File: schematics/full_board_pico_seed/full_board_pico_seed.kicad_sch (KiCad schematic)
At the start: 32 parts, among them J10 Conn_02x20_Odd_Even, J2 Conn_01x02_Male, J9 Conn_01x03, P0 25k, P1 25k, P2 25k, SW4 Enter, SW5 Exit, U12 128X64 OLED Display, U14 AP63205WU, U3 LM1117DT-5.0, U7 MC78M05_TO252

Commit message: minor corrections
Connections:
- net GND: no longer J10.10 (Pin_10), U12.4 (CS)
- new net: J10.10 (Pin_10), U12.4 (CS)
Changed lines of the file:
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@@
   (junction (at 142.24 134.62) (diameter 0) (color 0 0 0 0)
   )
-  (junction (at 62.23 121.92) (diameter 0) (color 0 0 0 0)
-  )
   (junction (at 208.28 72.39) (diameter 0) (color 0 0 0 0)
   )
   (junction (at 237.49 80.01) (diameter 0) (color 0 0 0 0)
-  )
-  (junction (at 62.23 125.73) (diameter 0) (color 0 0 0 0)
   )
   (junction (at 68.58 114.3) (diameter 0) (color 0 0 0 0)
@@
     (stroke (width 0) (type default))
   )
-  (wire (pts (xy 62.23 121.92) (xy 62.23 125.73))
+  (wire (pts (xy 62.23 102.87) (xy 62.23 181.61))
     (stroke (width 0) (type default))
   )
@@
     (stroke (width 0) (type default))
   )
+  (wire (pts (xy 59.69 121.92) (xy 57.15 121.92))
+    (stroke (width 0) (type default))
+  )
   (wire (pts (xy 52.07 128.27) (xy 40.64 128.27))
     (stroke (width 0) (type default))
@@
     (stroke (width 0) (type default))
   )
-  (wire (pts (xy 62.23 102.87) (xy 62.23 121.92))
-    (stroke (width 0) (type default))
-  )
   (wire (pts (xy 233.68 72.39) (xy 237.49 72.39))
     (stroke (width 0) (type default))
@@
     (stroke (width 0) (type default))
   )
-  (wire (pts (xy 62.23 125.73) (xy 62.23 181.61))
-    (stroke (width 0) (type default))
-  )
   (wire (pts (xy 90.17 118.11) (xy 105.41 118.11))
     (stroke (width 0) (type default))
@@
   )
   (wire (pts (xy 81.28 82.55) (xy 92.71 82.55))
-    (stroke (width 0) (type default))
-  )
-  (wire (pts (xy 62.23 121.92) (xy 57.15 121.92))
     (stroke (width 0) (type default))
   )
@@
     )
   )
-  (symbol (lib_id "power:GND") (at 62.23 125.73 0) (mirror y) (unit 1)
-    (in_bom yes) (on_board yes) (dnp no)
-    (property "Reference" "#PWR040" (at 62.23 132.08 0)
-      (effects (font (size 1.27 1.27)) hide)
-    )
-    (property "Value" "GND" (at 59.69 129.54 90)
-      (effects (font (size 1.27 1.27)))
-    )
-    (property "Footprint" "" (at 62.23 125.73 0)
-      (effects (font (size 1.27 1.27)) hide)
-    )
-    (property "Datasheet" "" (at 62.23 125.73 0)
-      (effects (font (size 1.27 1.27)) hide)
-    )
+  (symbol (lib_id "power:GND") (at 59.69 121.92 0) (mirror y) (unit 1)
+    (in_bom yes) (on_board yes) (dnp no)
+    (property "Reference" "#PWR040" (at 59.69 128.27 0)
+      (effects (font (size 1.27 1.27)) hide)
+    )
+    (property "Value" "GND" (at 59.69 120.65 0)
+      (effects (font (size 1.27 1.27)))
+    )
+    (property "Footprint" "" (at 59.69 121.92 0)
+      (effects (font (size 1.27 1.27)) hide)
+    )
+    (property "Datasheet" "" (at 59.69 121.92 0)
+      (effects (font (size 1.27 1.27)) hide)
+    )

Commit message: pcd: changed innductor footprint
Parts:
- L1: footprint Inductor_SMD:L_1812_4532Metric_Pad1.30x3.40mm_HandSolder -> Inductor_SMD:L_Bourns_SRP7028A_7.3x6.6mm
- U3: footprint Package_TO_SOT_SMD:TO-252-3_TabPin2 -> Package_TO_SOT_SMD:TO-252-2
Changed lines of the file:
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@@
       (effects (font (size 1.27 1.27)))
     )
-    (property "Footprint" "Inductor_SMD:L_1812_4532Metric_Pad1.30x3.40mm_HandSolder" (at 252.73 92.71 0)
+    (property "Footprint" "Inductor_SMD:L_Bourns_SRP7028A_7.3x6.6mm" (at 252.73 92.71 0)
       (effects (font (size 1.27 1.27)) hide)
     )
@@
       (effects (font (size 1.27 1.27)))
     )
-    (property "Footprint" "Package_TO_SOT_SMD:TO-252-3_TabPin2" (at 251.46 72.39 0)
-      (effects (font (size 1.27 1.27)) hide)
-    )
+    (property "Footprint" "Package_TO_SOT_SMD:TO-252-2" (at 251.46 72.39 0)
+      (effects (font (size 1.27 1.27)) hide)
+    )

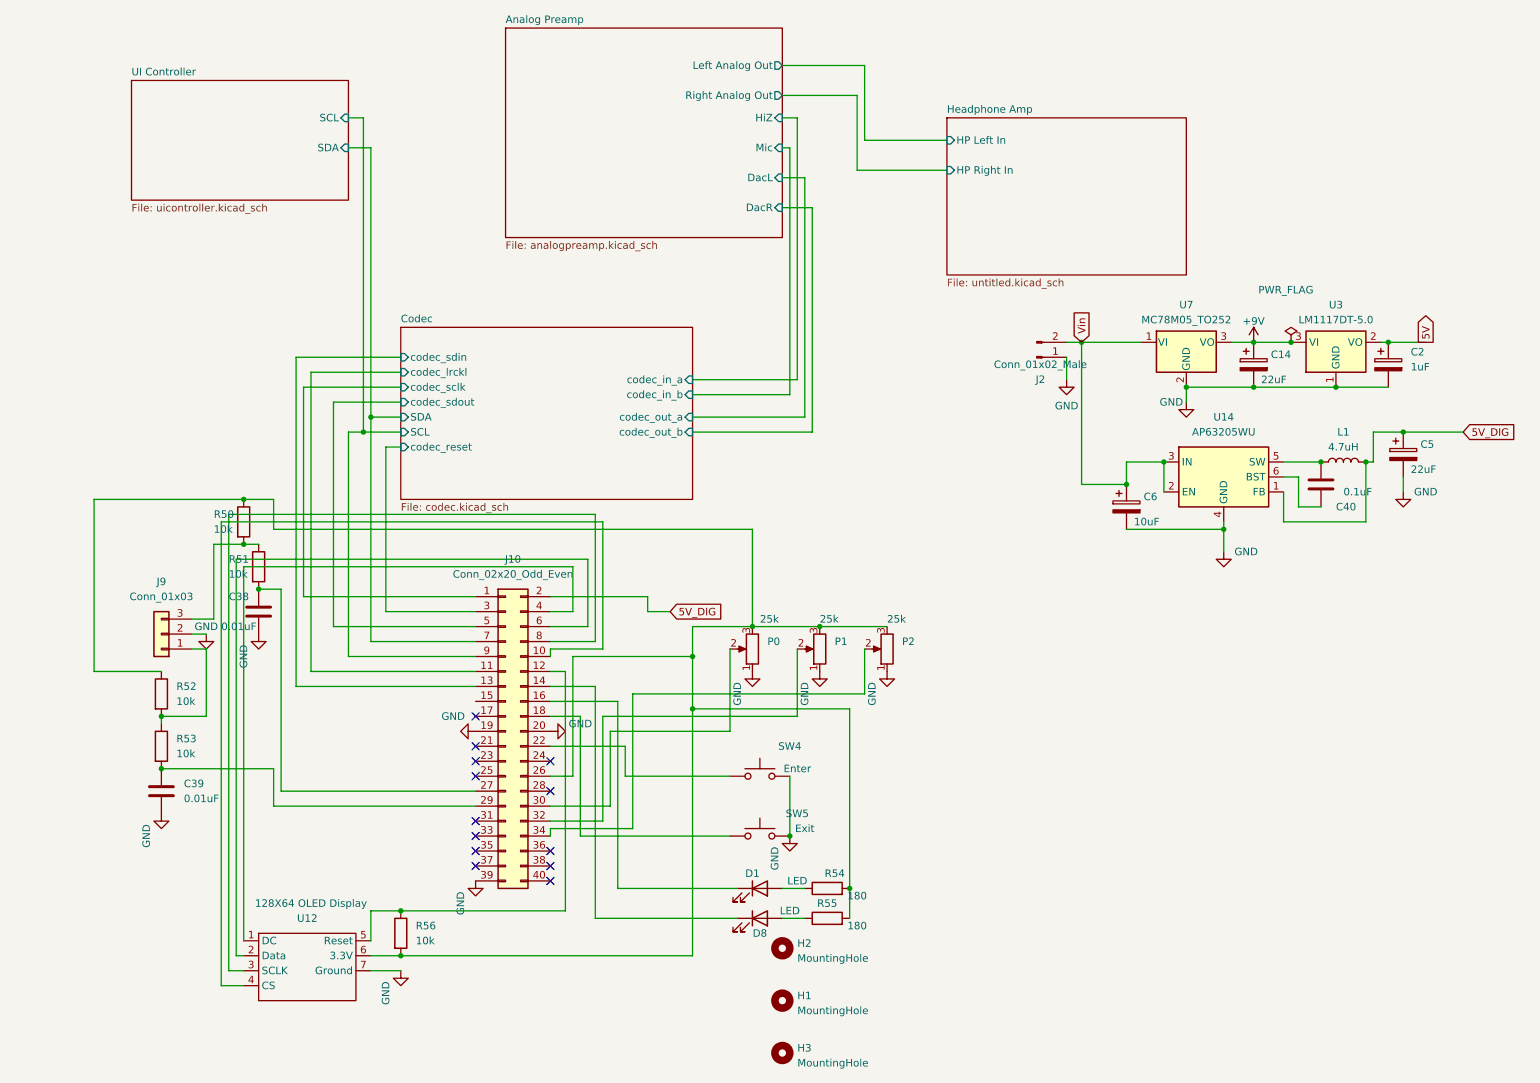
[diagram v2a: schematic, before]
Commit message: more work on full schematic: added test points
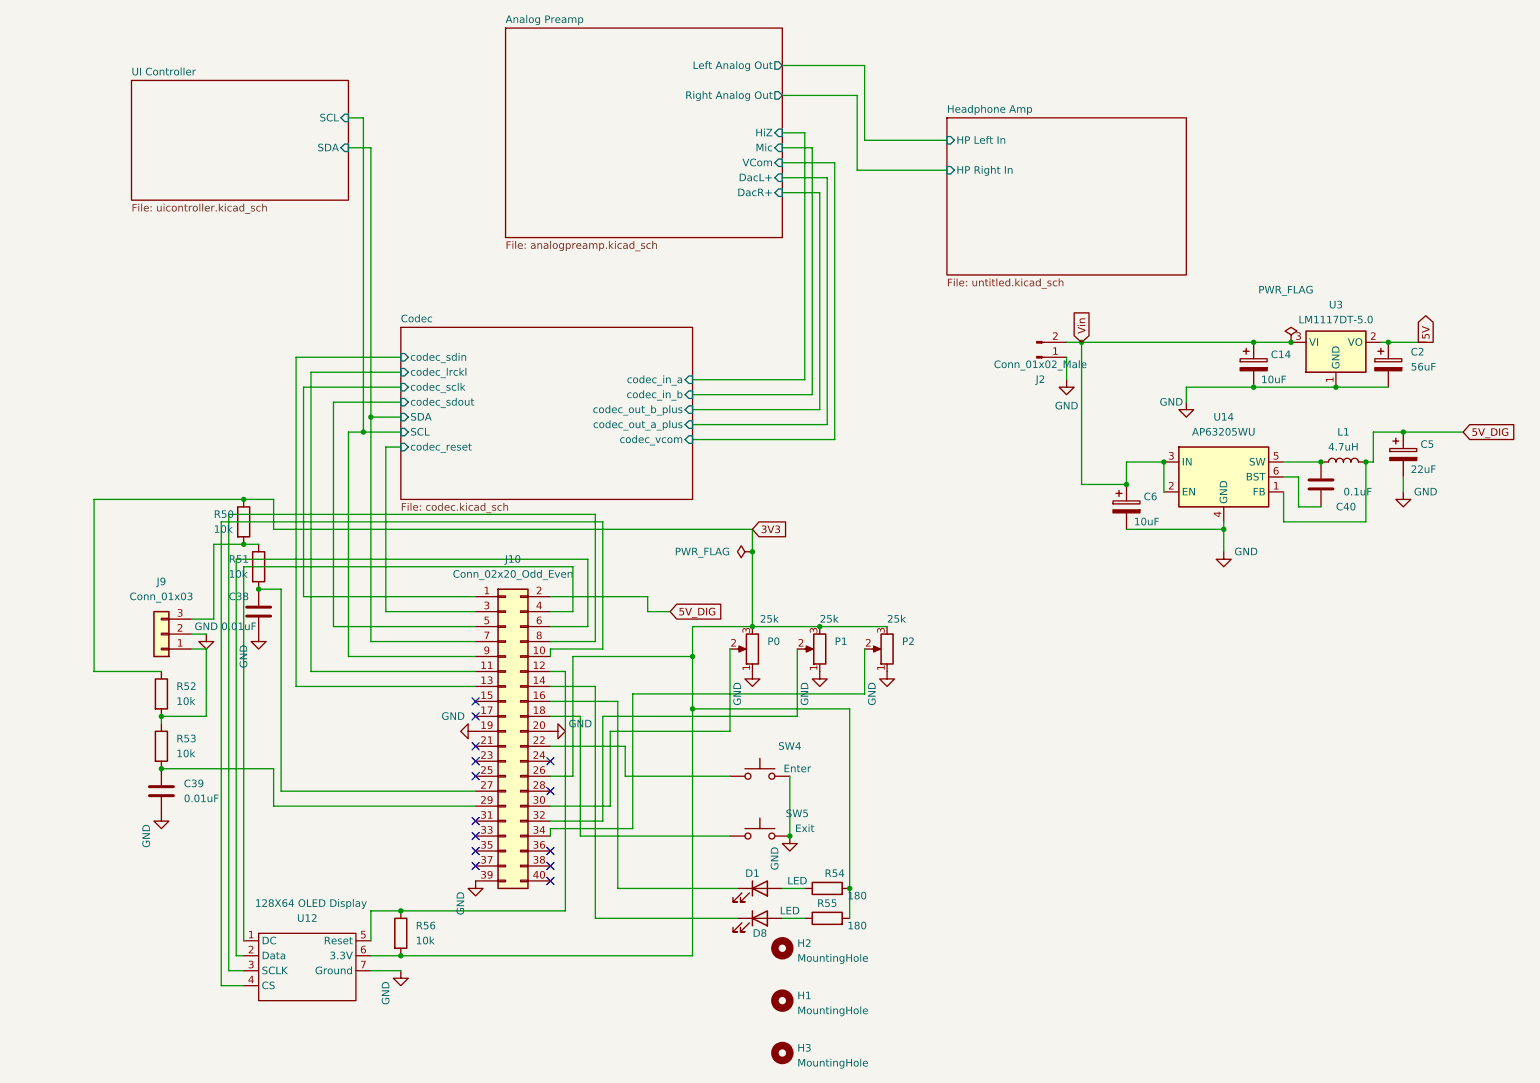
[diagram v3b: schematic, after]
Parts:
- removed U7: MC78M05_TO252, Package_TO_SOT_SMD:TO-252-2, symbol Regulator_Linear:MC78M05_TO252
- C14: value 22uF -> 10uF
- C2: value 1uF -> 56uF
- C40: footprint Capacitor_SMD:C_1210_3225Metric_Pad1.33x2.70mm_HandSolder -> Capacitor_SMD:C_0805_2012Metric_Pad1.18x1.45mm_HandSolder
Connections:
- net +9V is gone; now on net Vin: C14.1, U3.3 (VI)
- net 3V3: now reaches J10.26 (Pin_26), P0.3, P1.3, P2.3, R50.1, R52.1, R54.2, R55.2, R56.2, U12.6 (3.3V)
- no-connect marks 13 -> 14
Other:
- sheet Analog Preamp ports: added DacL+, DacR+, VCom; removed DacL, DacR
- sheet Codec ports: added codec_out_a_plus, codec_out_b_plus, codec_vcom; removed codec_out_a, codec_out_b

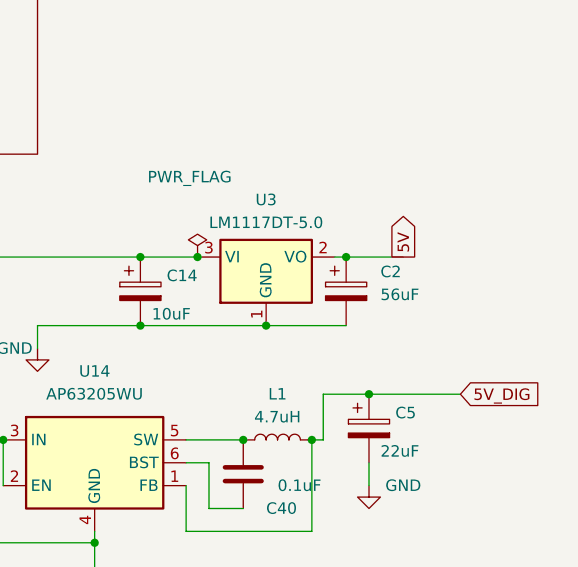
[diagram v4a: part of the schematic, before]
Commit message: worked on schematics
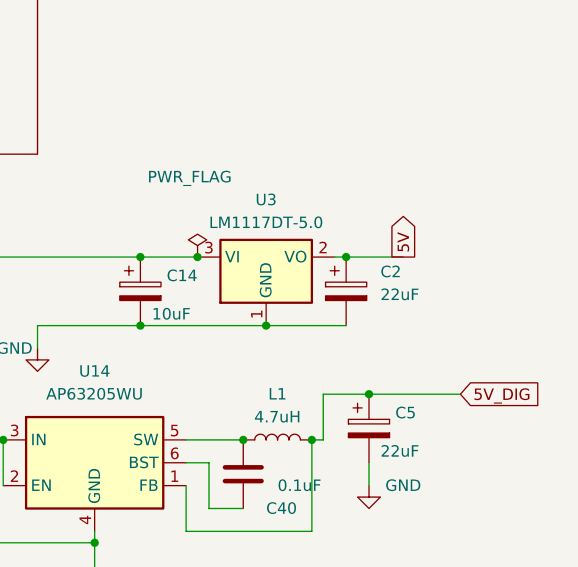
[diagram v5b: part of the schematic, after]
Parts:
- C2: value 56uF -> 22uF
- D1, D8, H1, H2, H3, J2, J9, P0, P1, P2, SW4, SW5, U12: now left out of the parts list
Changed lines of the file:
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@@
 		(unit 1)
 		(exclude_from_sim no)
-		(in_bom yes)
+		(in_bom no)
 		(on_board yes)
 		(dnp no)
@@
 		(unit 1)
 		(exclude_from_sim no)
-		(in_bom yes)
+		(in_bom no)
 		(on_board yes)
 		(dnp no)
@@
 		(unit 1)
 		(exclude_from_sim no)
-		(in_bom yes)
+		(in_bom no)
 		(on_board yes)
 		(dnp no)
@@
 		(unit 1)
 		(exclude_from_sim no)
-		(in_bom yes)
+		(in_bom no)
 		(on_board yes)
 		(dnp no)
@@
 		(unit 1)
 		(exclude_from_sim no)
-		(in_bom yes)
+		(in_bom no)
 		(on_board yes)
 		(dnp no)
@@
 		(unit 1)
 		(exclude_from_sim no)
-		(in_bom yes)
+		(in_bom no)
 		(on_board yes)
 		(dnp no)
@@
 		(unit 1)
 		(exclude_from_sim no)
-		(in_bom yes)
+		(in_bom no)
 		(on_board yes)
 		(dnp no)
@@
 		(unit 1)
 		(exclude_from_sim no)
-		(in_bom yes)
+		(in_bom no)
 		(on_board yes)
 		(dnp no)
@@
 		(unit 1)
 		(exclude_from_sim no)
-		(in_bom yes)
+		(in_bom no)
 		(on_board yes)
 		(dnp no)
@@
 		(fields_autoplaced yes)
 		(property "Reference" "C2"
-			(at 264.16 74.041 0)
+			(at 264.16 74.0409 0)
 			(effects
 				(font
@@
 			)
 		)
-		(property "Value" "56uF"
-			(at 264.16 76.581 0)
+		(property "Value" "22uF"
+			(at 264.16 76.5809 0)
 			(effects
 				(font
@@
 		(unit 1)
 		(exclude_from_sim no)
-		(in_bom yes)
+		(in_bom no)
 		(on_board yes)
 		(dnp no)
@@
 		(unit 1)
 		(exclude_from_sim no)
-		(in_bom yes)
+		(in_bom no)
 		(on_board yes)
 		(dnp no)
@@
 		(unit 1)
 		(exclude_from_sim no)
-		(in_bom yes)
+		(in_bom no)
 		(on_board yes)
 		(dnp no)
@@
 		(unit 1)
 		(exclude_from_sim no)
-		(in_bom yes)
-		(on_board yes)
-		(dnp no)
+		(in_bom no)
+		(on_board yes)
+		(dnp no)
